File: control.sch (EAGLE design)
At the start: 118 parts, among them IC1 LM358N, IC2 XMEGA16A4A, IC3 LM317MBSTT3, IC5 LM358N, Q1 BSS123, Q10 TIP42C, Q11 BC338, Q12 BC548, Q13 BC557C, Q14 BSS123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

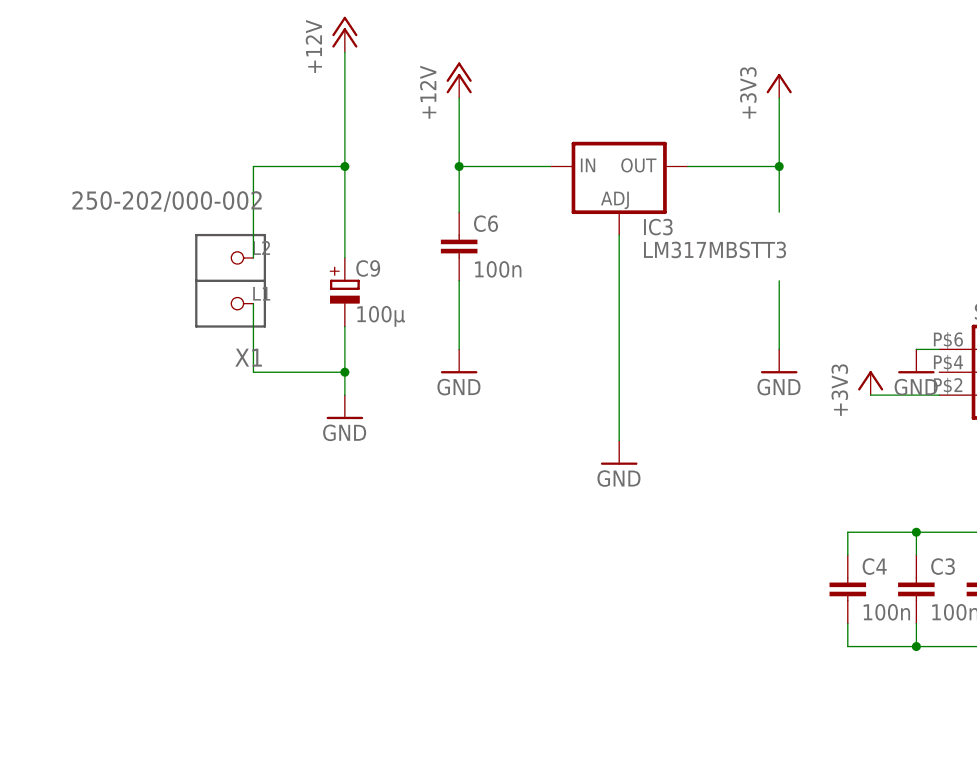
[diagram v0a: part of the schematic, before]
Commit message: power connector hohlstecker
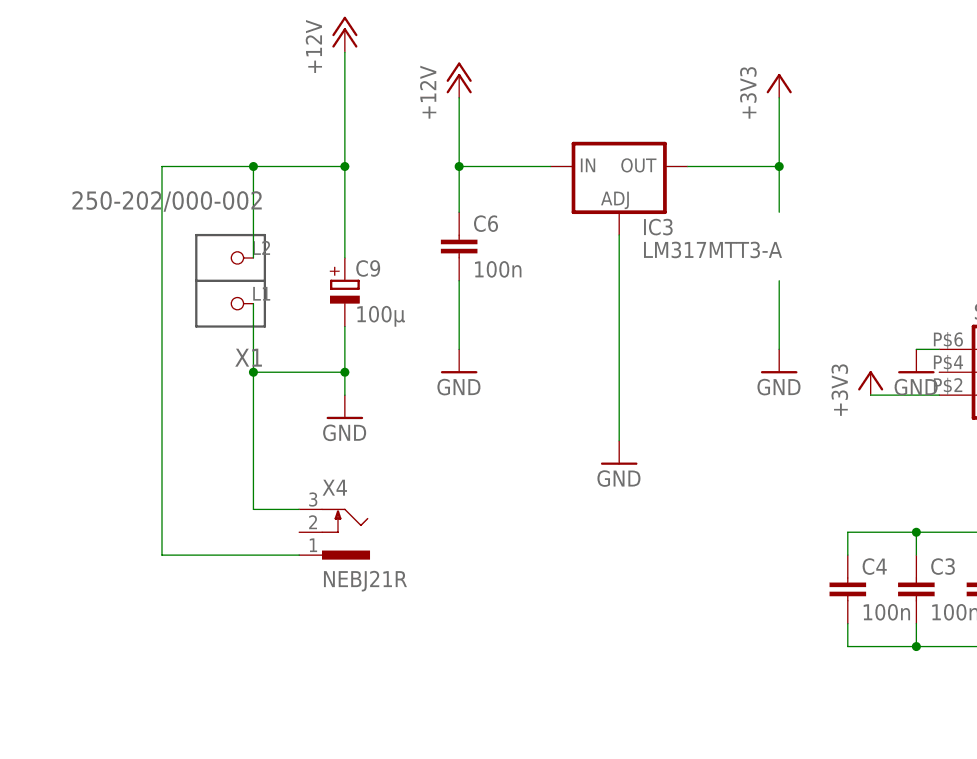
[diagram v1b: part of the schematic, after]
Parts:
- added X4: NEBJ21R, con-lumberg:NEBJ21R
- IC3: value LM317MBSTT3 -> LM317MTT3-A; device v-reg:LM317MBSTT3 -> v-reg:LM317MTT3-A
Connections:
- net +12V: now also X4.1
- net GND: now also X4.3
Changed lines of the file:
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@@
 <grid distance="0.1" unitdist="inch" unit="inch" style="lines" multiple="1" display="no" altdistance="0.01" altunitdist="inch" altunit="inch"/>
 <layers>
-<layer number="1" name="Top" color="4" fill="1" visible="no" active="no"/>
-<layer number="16" name="Bottom" color="1" fill="1" visible="no" active="no"/>
-<layer number="17" name="Pads" color="2" fill="1" visible="no" active="no"/>
-<layer number="18" name="Vias" color="2" fill="1" visible="no" active="no"/>
-<layer number="19" name="Unrouted" color="6" fill="1" visible="no" active="no"/>
-<layer number="20" name="Dimension" color="15" fill="1" visible="no" active="no"/>
-<layer number="21" name="tPlace" color="7" fill="1" visible="no" active="no"/>
-<layer number="22" name="bPlace" color="7" fill="1" visible="no" active="no"/>
-<layer number="23" name="tOrigins" color="15" fill="1" visible="no" active="no"/>
-<layer number="24" name="bOrigins" color="15" fill="1" visible="no" active="no"/>
-<layer number="25" name="tNames" color="7" fill="1" visible="no" active="no"/>
-<layer number="26" name="bNames" color="7" fill="1" visible="no" active="no"/>
-<layer number="27" name="tValues" color="7" fill="1" visible="no" active="no"/>
-<layer number="28" name="bValues" color="7" fill="1" visible="no" active="no"/>
+<layer number="1" name="Top" color="4" fill="1" visible="yes" active="no"/>
+<layer number="16" name="Bottom" color="1" fill="1" visible="yes" active="no"/>
+<layer number="17" name="Pads" color="2" fill="1" visible="yes" active="no"/>
+<layer number="18" name="Vias" color="2" fill="1" visible="yes" active="no"/>
+<layer number="19" name="Unrouted" color="6" fill="1" visible="yes" active="no"/>
+<layer number="20" name="Dimension" color="15" fill="1" visible="yes" active="no"/>
+<layer number="21" name="tPlace" color="7" fill="1" visible="yes" active="no"/>
+<layer number="22" name="bPlace" color="7" fill="1" visible="yes" active="no"/>
+<layer number="23" name="tOrigins" color="15" fill="1" visible="yes" active="no"/>
+<layer number="24" name="bOrigins" color="15" fill="1" visible="yes" active="no"/>
+<layer number="25" name="tNames" color="7" fill="1" visible="yes" active="no"/>
+<layer number="26" name="bNames" color="7" fill="1" visible="yes" active="no"/>
+<layer number="27" name="tValues" color="7" fill="1" visible="yes" active="no"/>
+<layer number="28" name="bValues" color="7" fill="1" visible="yes" active="no"/>
 <layer number="29" name="tStop" color="7" fill="3" visible="no" active="no"/>
 <layer number="30" name="bStop" color="7" fill="6" visible="no" active="no"/>
@@
 <layer number="35" name="tGlue" color="7" fill="4" visible="no" active="no"/>
 <layer number="36" name="bGlue" color="7" fill="5" visible="no" active="no"/>
-<layer number="37" name="tTest" color="7" fill="1" visible="no" active="no"/>
-<layer number="38" name="bTest" color="7" fill="1" visible="no" active="no"/>
+<layer number="37" name="tTest" color="7" fill="1" visible="yes" active="no"/>
+<layer number="38" name="bTest" color="7" fill="1" visible="yes" active="no"/>
 <layer number="39" name="tKeepout" color="4" fill="11" visible="no" active="no"/>
 <layer number="40" name="bKeepout" color="1" fill="11" visible="no" active="no"/>
@@
 <layer number="44" name="Drills" color="7" fill="1" visible="no" active="no"/>
 <layer number="45" name="Holes" color="7" fill="1" visible="no" active="no"/>
-<layer number="46" name="Milling" color="3" fill="1" visible="no" active="no"/>
-<layer number="47" name="Measures" color="7" fill="1" visible="no" active="no"/>
-<layer number="48" name="Document" color="7" fill="1" visible="no" active="no"/>
-<layer number="49" name="Reference" color="7" fill="1" visible="no" active="no"/>
-<layer number="51" name="tDocu" color="7" fill="1" visible="no" active="no"/>
-<layer number="52" name="bDocu" color="7" fill="1" visible="no" active="no"/>
+<layer number="46" name="Milling" color="3" fill="1" visible="yes" active="no"/>
+<layer number="47" name="Measures" color="7" fill="1" visible="yes" active="no"/>
+<layer number="48" name="Document" color="7" fill="1" visible="yes" active="no"/>
+<layer number="49" name="Reference" color="7" fill="1" visible="yes" active="no"/>
+<layer number="51" name="tDocu" color="7" fill="1" visible="yes" active="no"/>
+<layer number="52" name="bDocu" color="7" fill="1" visible="yes" active="no"/>
 <layer number="91" name="Nets" color="2" fill="1" visible="yes" active="yes"/>
 <layer number="92" name="Busses" color="1" fill="1" visible="yes" active="yes"/>
@@
 <part name="+3V1" library="supply1" deviceset="+3V3" device=""/>
 <part name="+3V3" library="supply1" deviceset="+3V3" device=""/>
-<part name="IC3" library="v-reg" deviceset="LM317?*" device="MBSTT3"/>
+<part name="IC3" library="v-reg" deviceset="LM317?*" device="MTT3-A" value="LM317MTT3-A"/>
 <part name="C6" library="resistor" deviceset="C-EU" device="C0805K" value="100n"/>
 <part name="GND10" library="supply1" deviceset="GND" device=""/>
@@
 <part name="R63" library="resistor" deviceset="R-EU_" device="M0805" value="33k"/>
 <part name="GND9" library="supply1" deviceset="GND" device=""/>
+<part name="X4" library="con-lumberg" deviceset="NEBJ21R" device=""/>
 </parts>
 <sheets>
@@
 <instance part="R63" gate="G$1" x="165.1" y="167.64"/>
 <instance part="GND9" gate="1" x="187.96" y="154.94"/>
+<instance part="X4" gate="G$1" x="12.7" y="215.9"/>
 </instances>
 <busses>
@@
 <wire x1="2.54" y1="233.68" x2="2.54" y2="241.3" width="0.1524" layer="91"/>
 <junction x="12.7" y="233.68"/>
+<wire x1="2.54" y1="233.68" x2="2.54" y2="218.44" width="0.1524" layer="91"/>
+<junction x="2.54" y="233.68"/>
+<pinref part="X4" gate="G$1" pin="3"/>
+<wire x1="2.54" y1="218.44" x2="7.62" y2="218.44" width="0.1524" layer="91"/>
 </segment>
 <segment>
@@
 <wire x1="2.54" y1="256.54" x2="12.7" y2="256.54" width="0.1524" layer="91"/>
 <junction x="12.7" y="256.54"/>
-</segment>
-<segment>
+<wire x1="2.54" y1="256.54" x2="-7.62" y2="256.54" width="0.1524" layer="91"/>
+<wire x1="-7.62" y1="256.54" x2="-7.62" y2="213.36" width="0.1524" layer="91"/>
+<junction x="2.54" y="256.54"/>
+<pinref part="X4" gate="G$1" pin="1"/>
+<wire x1="-7.62" y1="213.36" x2="7.62" y2="213.36" width="0.1524" layer="91"/>
+</segment>
+<segment>

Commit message: gnd vias
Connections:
- net GND: now also X4.2
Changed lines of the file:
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@@
 <pinref part="X4" gate="G$1" pin="3"/>
 <wire x1="2.54" y1="218.44" x2="7.62" y2="218.44" width="0.1524" layer="91"/>
+<pinref part="X4" gate="G$1" pin="2"/>
+<wire x1="7.62" y1="215.9" x2="2.54" y2="215.9" width="0.1524" layer="91"/>
+<wire x1="2.54" y1="215.9" x2="2.54" y2="218.44" width="0.1524" layer="91"/>
+<junction x="2.54" y="218.44"/>
 </segment>
 <segment>

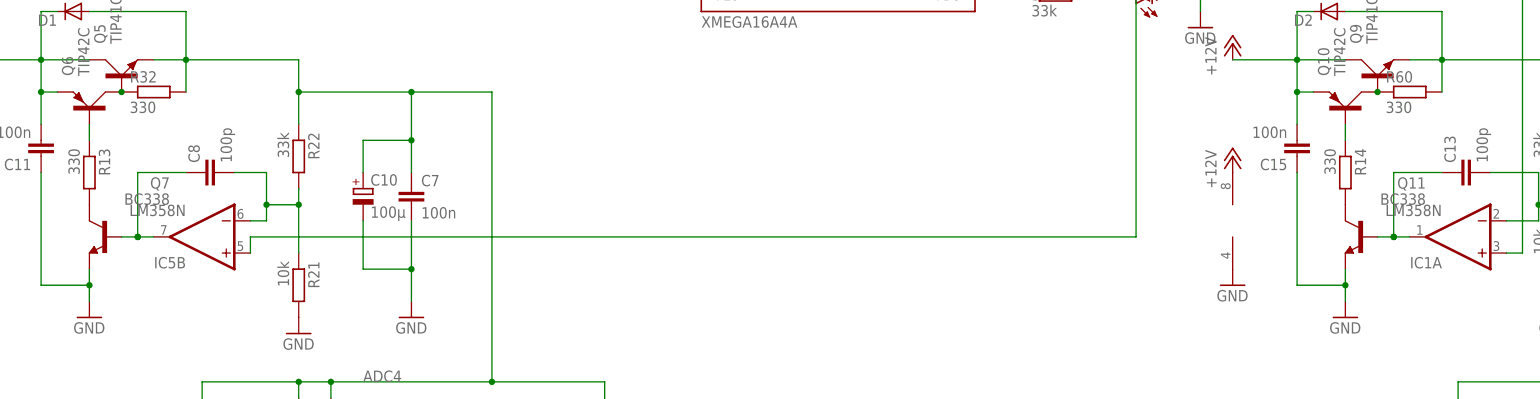
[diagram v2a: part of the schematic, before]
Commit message: transistor to bc548
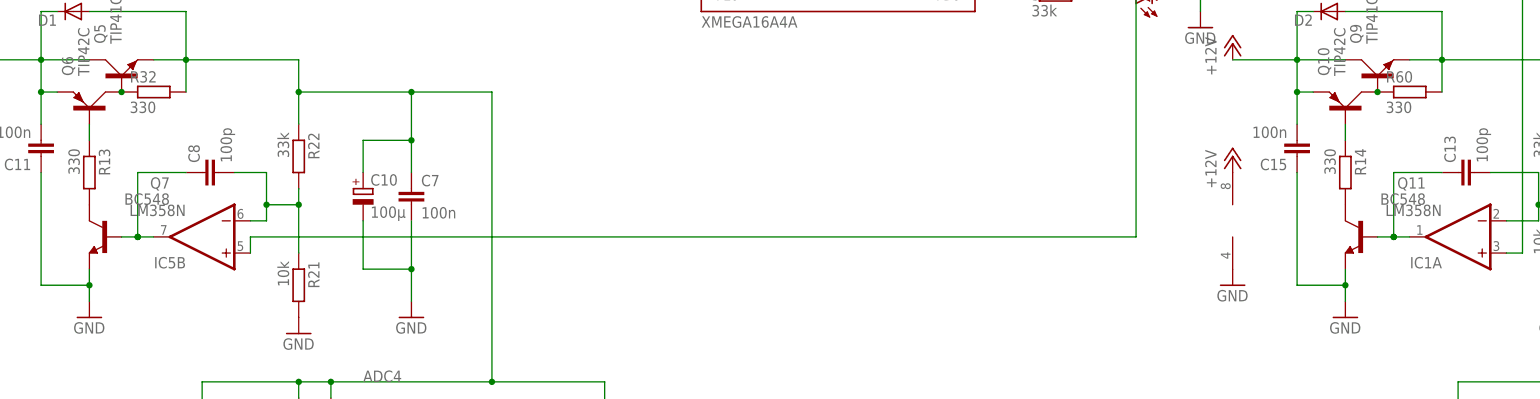
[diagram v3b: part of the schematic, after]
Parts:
- Q11, Q7: value BC338 -> BC548; device transistor-npn:BC338 -> transistor-npn:BC548
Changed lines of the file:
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@@
 <part name="Q5" library="transistor-power" deviceset="TIP41C" device=""/>
 <part name="Q6" library="transistor-power" deviceset="TIP42C" device=""/>
-<part name="Q7" library="transistor-npn" deviceset="BC338*" device=""/>
+<part name="Q7" library="transistor-npn" deviceset="BC548*" device=""/>
 <part name="R24" library="resistor" deviceset="R-EU_" device="0207/2V" value="1"/>
 <part name="R25" library="resistor" deviceset="R-EU_" device="0207/2V" value="1"/>
@@
 <part name="Q9" library="transistor-power" deviceset="TIP41C" device=""/>
 <part name="Q10" library="transistor-power" deviceset="TIP42C" device=""/>
-<part name="Q11" library="transistor-npn" deviceset="BC338*" device=""/>
+<part name="Q11" library="transistor-npn" deviceset="BC548*" device=""/>
 <part name="R49" library="resistor" deviceset="R-EU_" device="0207/2V" value="1"/>
 <part name="R50" library="resistor" deviceset="R-EU_" device="0207/2V" value="1"/>
